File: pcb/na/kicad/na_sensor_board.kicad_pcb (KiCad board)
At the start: 2 copper layers, 66.3 x 125.8 mm, 15 parts, among them J1 5V in (FFC), J2 55909-2474, U1 SHT40, U2 ADAU7002

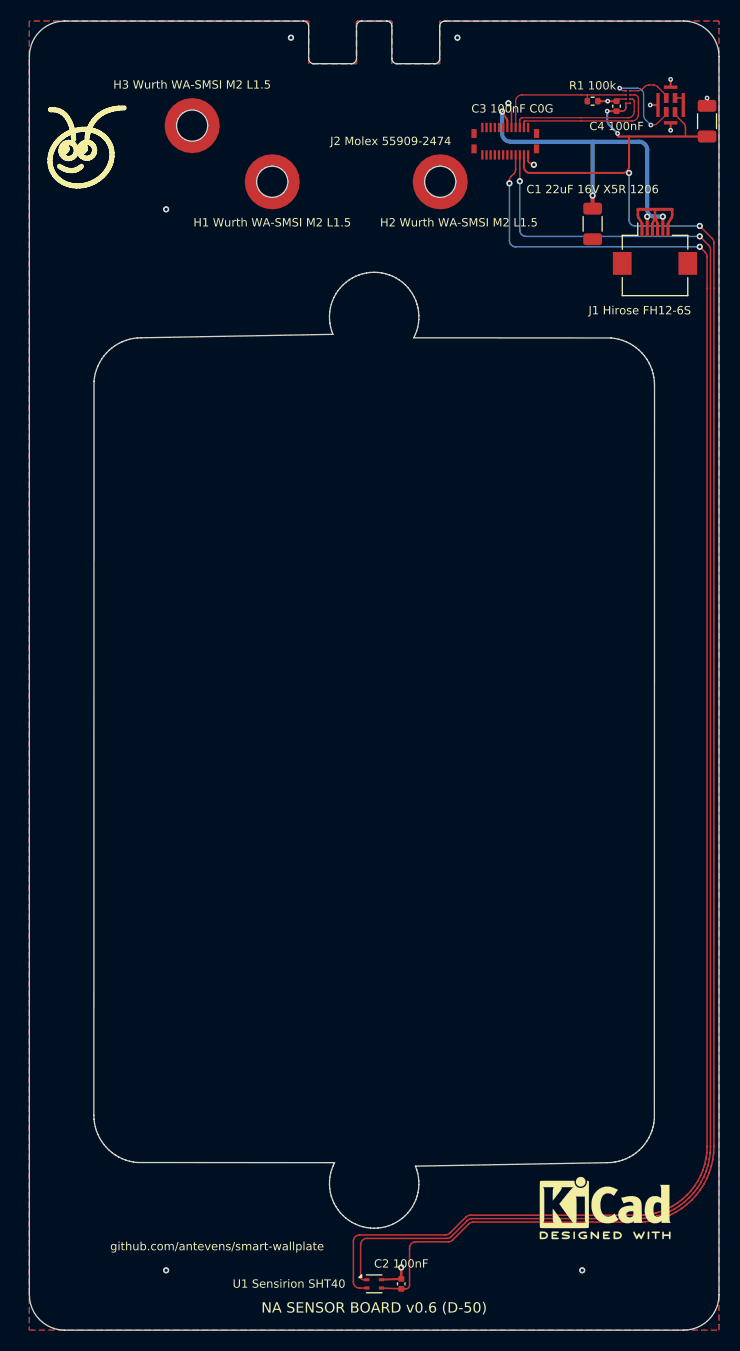
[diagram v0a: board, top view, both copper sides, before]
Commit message: v0.6: one barrier per variant, EU ridges, NA cable slit, ElegooSlicer projects, back cover and plate fixes (D-127..D-150)
- One barrier per variant for every edition; printed blank board in switch only (D-127..D-131)
- EU pin board ridge loop and blank board ridge; more pin board bosses (D-128..D-133)
- NA face plate lobes round the screws form the pocket's ends (D-132)
- NA 5 V cable straight from J2 to J1 through a slit in the barrier's bottom wall, 50 mm FFC; MH3 back in line;
  slit open in battery-free and switch only (D-134, D-135)
- Back cover: flex pad section 1.5 mm in, rim cut at the bottom end with a 0.08 mm-layer taper, steel plate clips
  solid in the shell, bottom clip lead-in 45 deg, pry notch 1.5 deep (D-136..D-143, D-145, D-147)
- 45 deg chamfer round the remote pocket's mouth (D-139)
- Print projects built with ElegooSlicer 1.5.3.5, overrides also as object settings (D-144)
- EU plain face plate 84.6 x 84.6, plain carrier whole on all sides with the full rim (D-146, D-150)
- Steel piece 1.0 mm thick, recess 1.2 deep (D-148)
- MSR-2 12 mm left, grille on the plate's centre line; ant logos in the sensor boards' lower-left corners (D-149)
- Repo URL github.com/antevens/sladdseg on the boards
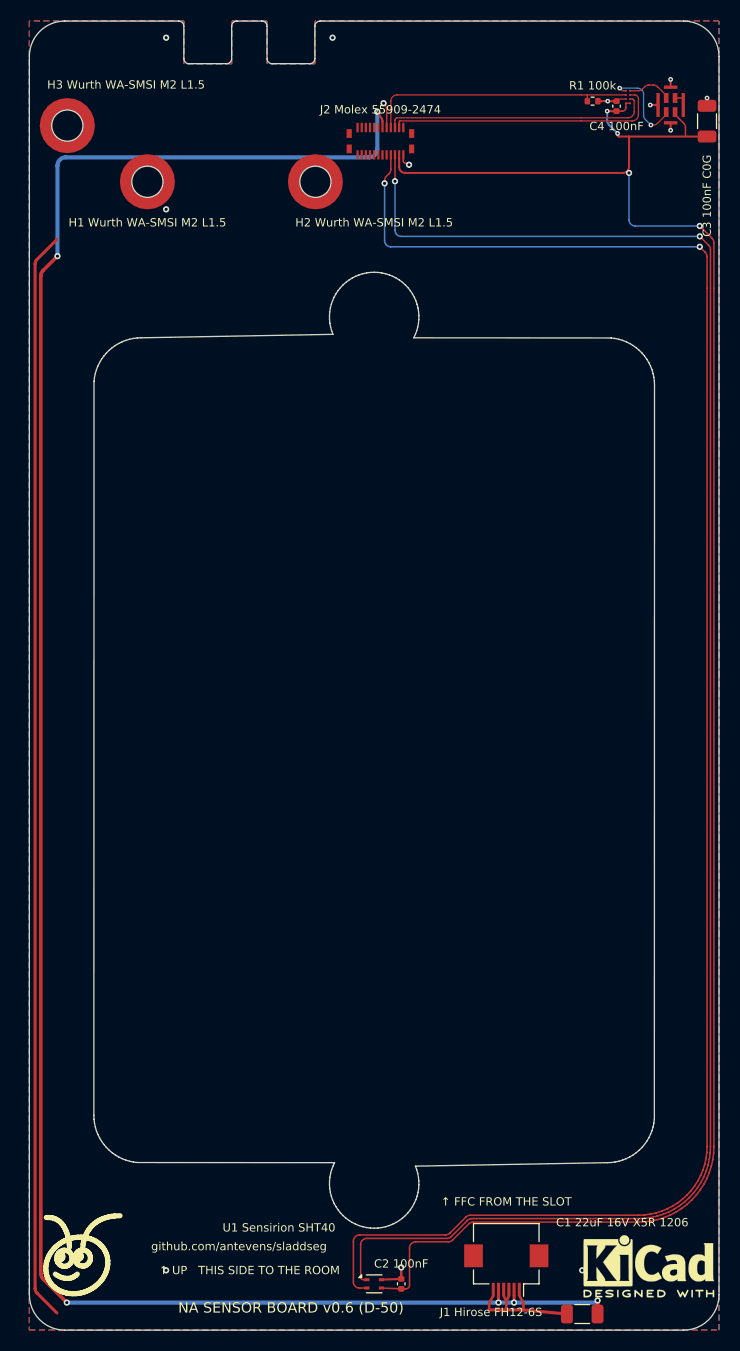
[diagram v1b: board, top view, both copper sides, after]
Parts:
- moved LOGO1 106.5 mm to (72.0, 148.5)
- moved C1 104.8 mm to (120.0, 154.2), turned to 180 degrees
- moved J1 99.2 mm to (112.7, 150.0), turned to 180 degrees
- moved H1 12.0 mm to (78.2, 45.4)
- moved H2 12.0 mm to (94.3, 45.4)
- moved H3 12.0 mm to (70.5, 40.0)
- moved J2 12.0 mm to (100.6, 41.5)
- moved LOGO2 7.00 mm to (126.4, 149.6)
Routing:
- net +5V: track 33.4 -> 201.1 mm, vias 4 -> 6
- net GND: track 20.5 -> 129.6 mm
- net /SDA: track 154.8 -> 166.8 mm
- net /SCL: track 157.7 -> 169.7 mm
- net /I2S_SCK: track 14.0 -> 26.0 mm
- net /I2S_WS: track 13.2 -> 25.2 mm
- net /I2S_SD: track 13.6 -> 25.6 mm
- net +3V3: track 172.8 -> 184.8 mm
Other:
- outline, holes or cut-outs redrawn
- board text added: "THIS SIDE TO THE WALL ↑ UP"
- board text added: "github.com/antevens/sladdseg"
- board text added: "↑ FFC FROM THE SLOT"
- board text added: "↑ UP THIS SIDE TO THE ROOM"
- board text removed: "github.com/antevens/smart-wallplate"

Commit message: Version v0.7 (D-151): boards, fab and PCBWay packs, order upload name and section renders renamed; v0.6 files removed
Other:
- board text added: "NA SENSOR BOARD v0.7 (D-50)"
- board text removed: "NA SENSOR BOARD v0.6 (D-50)"
